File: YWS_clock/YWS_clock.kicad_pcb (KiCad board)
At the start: 2 copper layers, 140 x 90 mm, 60 parts, among them J1 Conn_01x06, J2 Power_inlet_vertical, J3 Conn_01x06, J4 Conn_01x06, SW1 Omron_B3F_SPST, SW2 Omron_B3F_SPST, SW3 Omron_B3F_SPST, SW4 Omron_B3F_SPST, U1 L7805, U2 ATmega328-PU, U3 DS1307_DIP-8, U4 MAX7219, U5 MAX7219, U6 MAX7219, U7 MAX7219, Y1 Crystal_16MHz, Y2 Crystal_16MHz

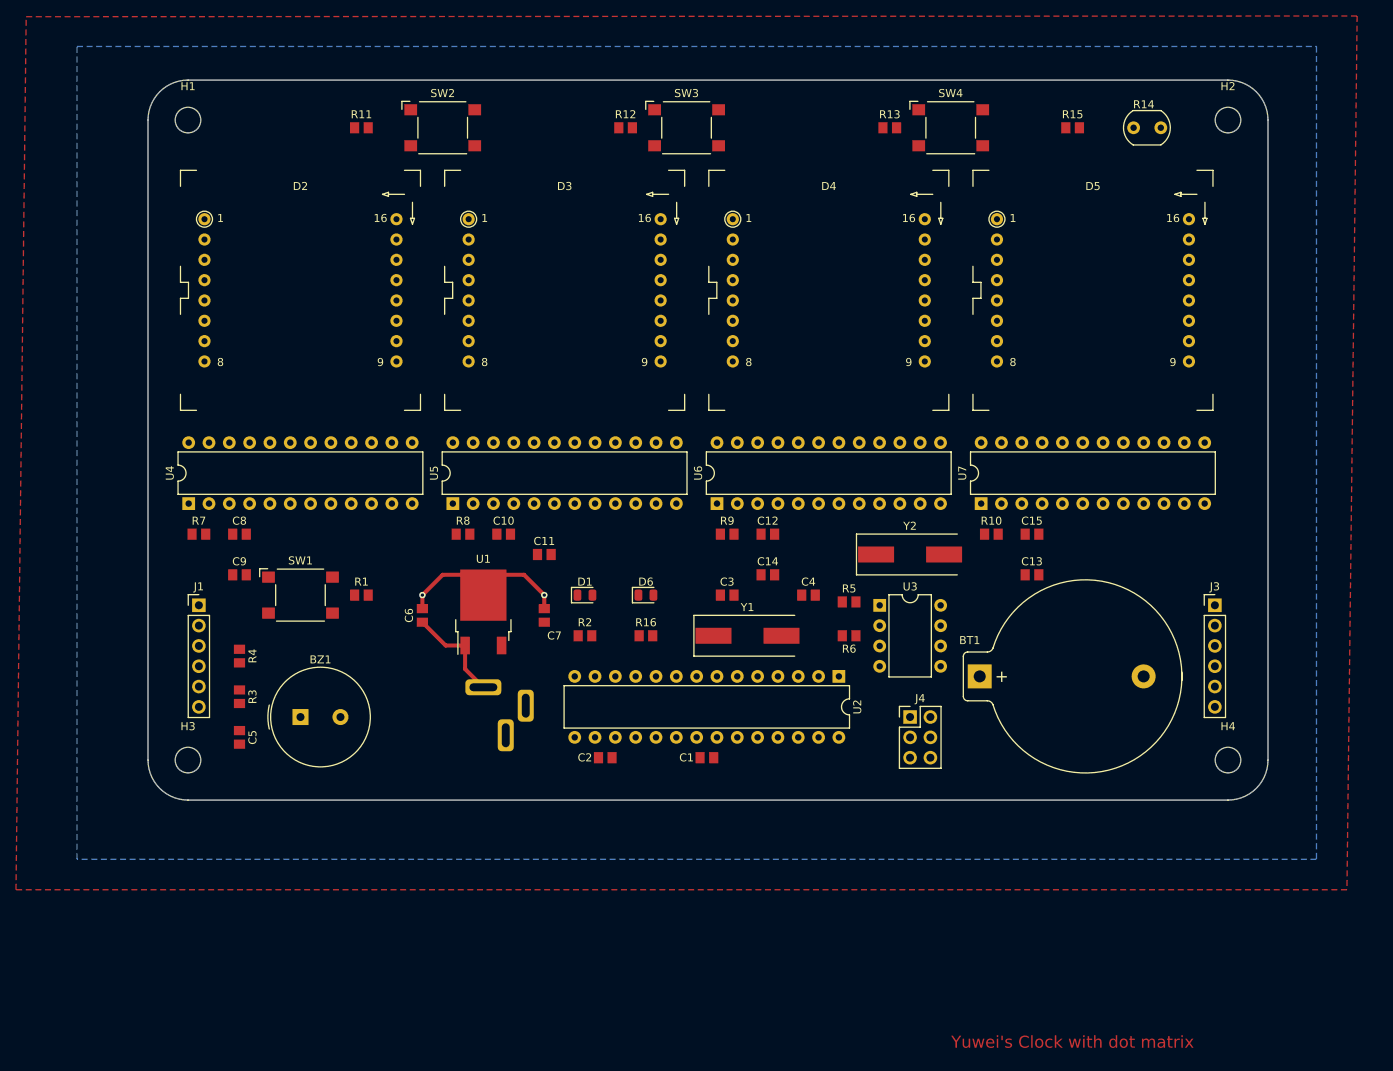
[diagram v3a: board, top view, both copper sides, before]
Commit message: Initial version with full routing and test point
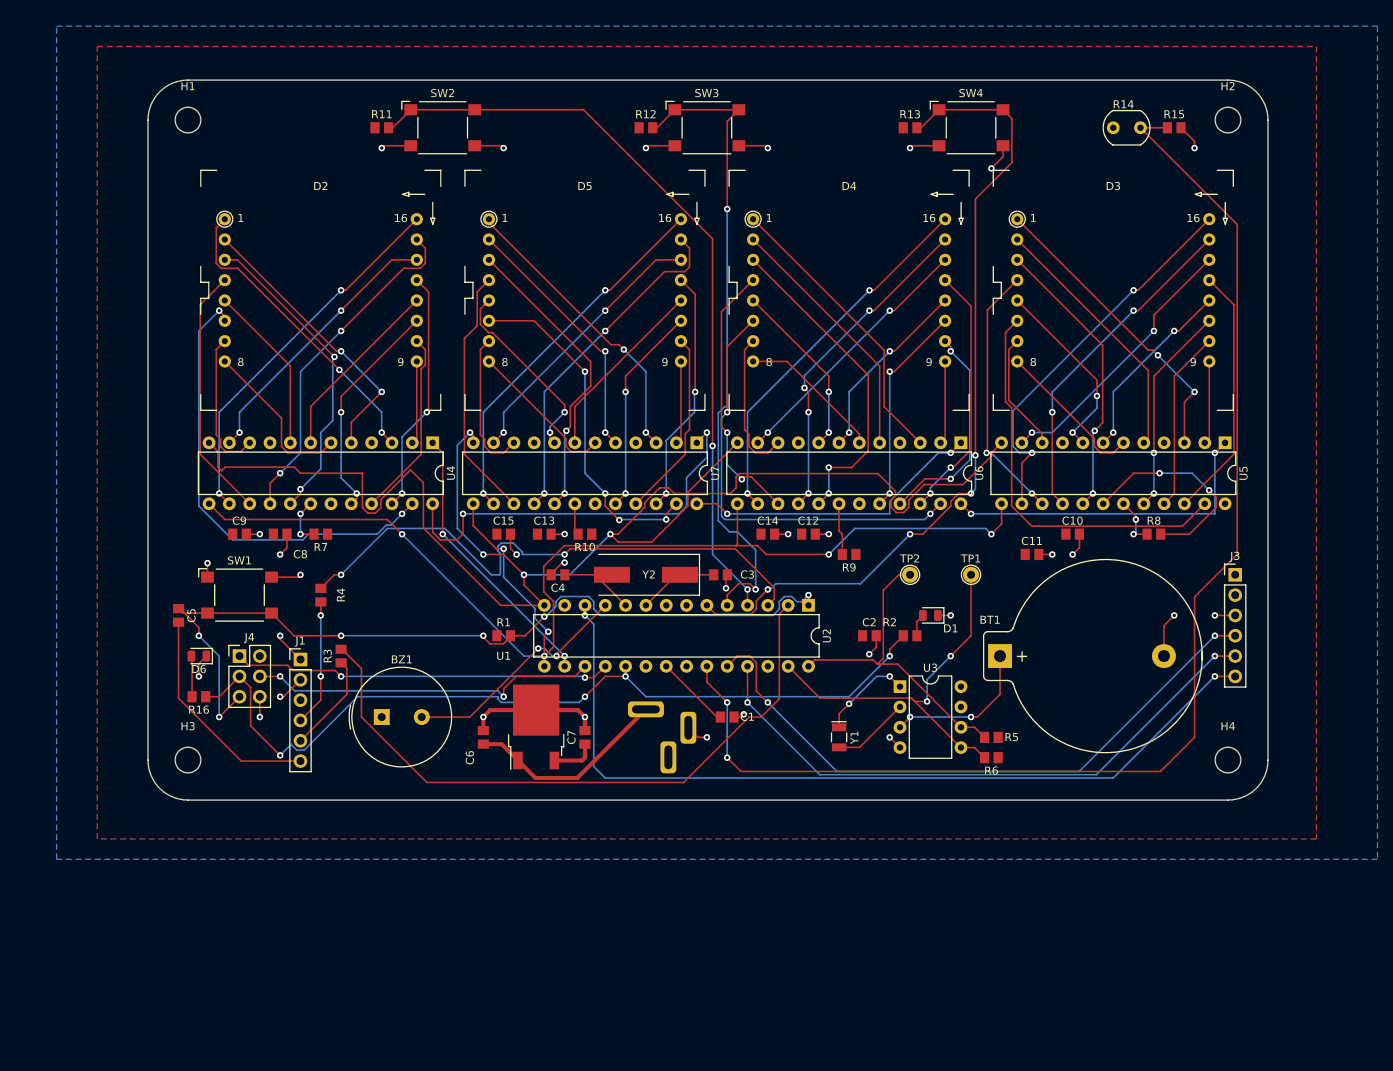
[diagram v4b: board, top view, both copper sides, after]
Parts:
- added TP1: TestPoint, footprints:TestPoint_THTPad_D2.0mm_Drill1.0mm, F.Cu at (182.9, 116.8)
- added TP2: TestPoint, footprints:TestPoint_THTPad_D2.0mm_Drill1.0mm, F.Cu at (175.3, 116.8)
- Y1: value Crystal_16MHz -> Crystal_32768Hz; footprint footprints:Crystal_SMD_HC49-SD -> footprints:Crystal_SMD_2Pin_3.2x1.5mm
- moved U5 96.8 mm to (214.6, 100.3), turned to -90 degrees
- moved R8 86.4 mm to (205.7, 111.8)
- moved J4 84.2 mm to (91.4, 127.0)
- moved C10 71.1 mm to (195.6, 111.8)
- moved D3 68.6 mm to (200.7, 81.3)
- moved C15 66.0 mm to (124.5, 111.8)
- moved D5 63.5 mm to (134.6, 81.3)
- moved C13 61.2 mm to (129.5, 111.8)
- moved C11 61.0 mm to (190.5, 114.3)
- moved D6 56.4 mm to (86.4, 127.0), turned to 180 degrees
- moved R16 56.4 mm to (86.4, 132.1), turned to 180 degrees
- moved R10 50.8 mm to (134.6, 111.8), turned to 180 degrees
- moved D1 43.3 mm to (177.8, 121.9), turned to 180 degrees
- moved R2 40.6 mm to (175.3, 124.5)
- moved C2 36.4 mm to (170.2, 124.5)
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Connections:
- J3 pad 6: JOYST_Z -> JOYST_SW
- J4 pad 1: MISD -> MISO
- J4 pad 4: MDSI -> MOSI
- U2 pad 11: JOYST_X -> BUZZER
- U2 pad 12: JOYST_Y -> JOYST_SW
- U2 pad 13: JOYST_Z -> unconnected-(U2-Pad13)
- U2 pad 24: BUZZER -> JOYST_X
- U2 pad 25: unconnected-(U2-Pad25) -> JOYST_Y
- Y1 pad 1: Net-(C3-Pad1) -> Net-(U3-Pad1)
- Y1 pad 2: Net-(C4-Pad1) -> Net-(U3-Pad2)
- Y2 pad 1: Net-(U3-Pad1) -> Net-(C3-Pad1)
- Y2 pad 2: Net-(U3-Pad2) -> Net-(C4-Pad1)
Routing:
- net DISP_LOAD: track 0.00 -> 189.8 mm, vias 0 -> 4
- net LIGHT_SENSOR: track 0.00 -> 160.2 mm, vias 0 -> 2
- net DISP_CLK: track 0.00 -> 157.0 mm, vias 0 -> 6
- net RESET: track 0.00 -> 107.8 mm, vias 0 -> 6
- net JOYST_SW: track 0.00 -> 106.6 mm, vias 0 -> 2
- net LED_SCK: track 0.00 -> 106.6 mm, vias 0 -> 4
- net BTN_DOWN: track 0.00 -> 103.3 mm, vias 0 -> 4
- net BTN_SEL: track 0.00 -> 95.7 mm, vias 0 -> 2
- net RXD: track 0.00 -> 81.7 mm
- net BTN_UP: track 0.00 -> 81.1 mm, vias 0 -> 2
- net JOYST_X: track 0.00 -> 79.1 mm, vias 0 -> 2
- net GND: track 22.8 -> 100.2 mm, vias 2 -> 32
- net JOYST_Y: track 0.00 -> 75.4 mm, vias 0 -> 2
- net TXD: track 0.00 -> 71.9 mm, vias 0 -> 2
- net Net-(D2-Pad6): track 0.00 -> 57.3 mm, vias 0 -> 2
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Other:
- board text removed: "Yuwei's Clock with dot matrix"

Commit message: Update with gerbers and BOM
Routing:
- net LED_SCK: track 106.6 -> 105.6 mm
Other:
- board text added: "RedSun"
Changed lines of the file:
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@@
     )
     (pad_to_mask_clearance 0)
+    (aux_axis_origin 78.74 144.78)
     (pcbplotparams
       (layerselection 0x00010fc_ffffffff)
@@
       (viasonmask false)
       (mode 1)
-      (useauxorigin false)
+      (useauxorigin true)
       (hpglpennumber 1)
       (hpglpenspeed 20)
@@
       (psa4output false)
       (plotreference true)
-      (plotvalue true)
+      (plotvalue false)
       (plotinvisibletext false)
       (sketchpadsonfab false)
-      (subtractmaskfromsilk false)
+      (subtractmaskfromsilk true)
       (outputformat 1)
       (mirror false)
-      (drillshape 1)
+      (drillshape 0)
       (scaleselection 1)
       (outputdirectory "")
@@
   (gr_line locked (start 210.6 57) (end 150 57) (layer "User.4") (width 0.05))
   (gr_line locked (start 82 64.4) (end 85 64.4) (layer "User.4") (width 0.05))
+  (gr_text "RedSun" (at 111.76 119.38) (layer "F.Cu")
+    (effects (font (size 2.286 2.286) (thickness 0.3) italic))
+  )
   (segment (start 95.44 117.13) (end 98.77 117.13) (width 0.2032) (layer "F.Cu") (net 1))
   (segment (start 152.252809 117.007191) (end 152.42 116.84) (width 0.2032) (layer "F.Cu") (net 1))
@@
   (segment (start 132.1 116.84) (end 135.88 116.84) (width 0.2032) (layer "F.Cu") (net 7))
   (segment (start 122.730689 125.464311) (end 124.430689 125.464311) (width 0.2032) (layer "F.Cu") (net 8))
-  (segment (start 91.44 132.08) (end 88.9 134.62) (width 0.2032) (layer "F.Cu") (net 8))
   (segment (start 125.31 124.585) (end 125.31 124.46) (width 0.2032) (layer "F.Cu") (net 8))
   (segment (start 84.003622 121.07) (end 83.82 121.07) (width 0.2032) (layer "F.Cu") (net 8))
@@
   (segment (start 127.149103 124.46) (end 129.54 122.069103) (width 0.2032) (layer "F.Cu") (net 8))
   (segment (start 124.430689 125.464311) (end 125.31 124.585) (width 0.2032) (layer "F.Cu") (net 8))
+  (segment (start 91.44 132.08) (end 88.9 134.62) (width 0.2032) (layer "F.Cu") (net 8))
   (segment (start 121.92 124.46) (end 121.92 124.653622) (width 0.2032) (layer "F.Cu") (net 8))
   (segment (start 87.44 121.63) (end 84.38 121.63) (width 0.2032) (layer "F.Cu") (net 8))
@@
   (segment (start 158.113111 121.92) (end 158.915689 121.117422) (width 0.2032) (layer "B.Cu") (net 8))
   (segment (start 129.54 122.069103) (end 129.69263 122.069103) (width 0.2032) (layer "B.Cu") (net 8))
+  (segment (start 88.9 127) (end 86.36 124.46) (width 0.2032) (layer "B.Cu") (net 8))
+  (segment (start 88.9 134.62) (end 88.9 127) (width 0.2032) (layer "B.Cu") (net 8))
   (segment (start 160.477422 119.555689) (end 161.124311 120.202578) (width 0.2032) (layer "B.Cu") (net 8))
   (segment (start 135.077422 119.555689) (end 135.724311 120.202578) (width 0.2032) (layer "B.Cu") (net 8))
@@
   (segment (start 131.622578 119.555689) (end 135.077422 119.555689) (width 0.2032) (layer "B.Cu") (net 8))
   (segment (start 104.14 124.46) (end 121.92 124.46) (width 0.2032) (layer "B.Cu") (net 8))
-  (segment (start 88.9 134.62) (end 88.9 127) (width 0.2032) (layer "B.Cu") (net 8))
-  (segment (start 88.9 127) (end 86.36 124.46) (width 0.2032) (layer "B.Cu") (net 8))
   (segment (start 158.915689 121.117422) (end 158.915689 120.202578) (width 0.2032) (layer "B.Cu") (net 8))
   (segment (start 161.124311 120.202578) (end 161.737422 120.202578) (width 0.2032) (layer "B.Cu") (net 8))
@@
   (segment (start 88.9 132.08) (end 91.44 129.54) (width 0.2032) (layer "F.Cu") (net 82))
   (segment (start 92.825689 130.925689) (end 92.825689 135.719989) (width 0.2032) (layer "F.Cu") (net 82))
+  (segment (start 92.825689 135.719989) (end 93.98 136.8743) (width 0.2032) (layer "F.Cu") (net 82))
   (segment (start 137.16 129.54) (end 139.7 129.54) (width 0.2032) (layer "F.Cu") (net 82))
   (segment (start 87.21 132.08) (end 88.9 132.08) (width 0.2032) (layer "F.Cu") (net 82))
   (segment (start 134.62 132.08) (end 137.16 129.54) (width 0.2032) (layer "F.Cu") (net 82))
-  (segment (start 92.825689 135.719989) (end 96.52 139.4143) (width 0.2032) (layer "F.Cu") (net 82))
+  (segment (start 93.98 136.8743) (end 93.98 137.16) (width 0.2032) (layer "F.Cu") (net 82))
   (segment (start 172.72 126.15) (end 172.72 127) (width 0.2032) (layer "F.Cu") (net 82))
   (segment (start 139.7 129.54) (end 139.7 128.28) (width 0.2032) (layer "F.Cu") (net 82))
@@
   (via (at 139.7 129.54) (size 0.8128) (drill 0.4064) (layers "F.Cu" "B.Cu") (net 82))
   (via (at 134.62 132.08) (size 0.8128) (drill 0.4064) (layers "F.Cu" "B.Cu") (net 82))
-  (via (at 96.52 139.4143) (size 0.8128) (drill 0.4064) (layers "F.Cu" "B.Cu") (net 82))
+  (via (at 93.98 137.16) (size 0.8128) (drill 0.4064) (layers "F.Cu" "B.Cu") (net 82))
   (via (at 172.72 127) (size 0.8128) (drill 0.4064) (layers "F.Cu" "B.Cu") (net 82))
   (segment (start 172.72 127) (end 167.64 132.08) (width 0.2032) (layer "B.Cu") (net 82))
   (segment (start 142.24 132.08) (end 139.7 129.54) (width 0.2032) (layer "B.Cu") (net 82))
+  (segment (start 99.538132 138.739311) (end 106.197443 132.08) (width 0.2032) (layer "B.Cu") (net 82))
+  (segment (start 95.559311 138.739311) (end 99.538132 138.739311) (width 0.2032) (layer "B.Cu") (net 82))
+  (segment (start 124.165613 132.790711) (end 133.909289 132.790711) (width 0.2032) (layer "B.Cu") (net 82))
+  (segment (start 123.749289 132.08) (end 123.749289 132.374387) (width 0.2032) (layer "B.Cu") (net 82))
+  (segment (start 167.64 132.08) (end 142.24 132.08) (width 0.2032) (layer "B.Cu") (net 82))
   (segment (start 106.197443 132.08) (end 123.749289 132.08) (width 0.2032) (layer "B.Cu") (net 82))
+  (segment (start 93.98 137.16) (end 95.559311 138.739311) (width 0.2032) (layer "B.Cu") (net 82))
   (segment (start 133.909289 132.790711) (end 134.62 132.08) (width 0.2032) (layer "B.Cu") (net 82))
-  (segment (start 97.905689 138.063132) (end 98.581868 138.739311) (width 0.2032) (layer "B.Cu") (net 82))
-  (segment (start 167.64 132.08) (end 142.24 132.08) (width 0.2032) (layer "B.Cu") (net 82))
-  (segment (start 98.581868 138.739311) (end 99.538132 138.739311) (width 0.2032) (layer "B.Cu") (net 82))
-  (segment (start 99.538132 138.739311) (end 106.197443 132.08) (width 0.2032) (layer "B.Cu") (net 82))
   (segment (start 123.749289 132.374387) (end 124.165613 132.790711) (width 0.2032) (layer "B.Cu") (net 82))
-  (segment (start 123.749289 132.08) (end 123.749289 132.374387) (width 0.2032) (layer "B.Cu") (net 82))
-  (segment (start 96.52 139.4143) (end 97.905689 138.028611) (width 0.2032) (layer "B.Cu") (net 82))
-  (segment (start 124.165613 132.790711) (end 133.909289 132.790711) (width 0.2032) (layer "B.Cu") (net 82))
-  (segment (start 97.905689 138.028611) (end 97.905689 138.063132) (width 0.2032) (layer "B.Cu") (net 82))
   (segment (start 155.133622 134.62) (end 146.955302 142.79832) (width 0.2032) (layer "F.Cu") (net 83))
   (segment (start 104.265 126.15) (end 104.14 126.15) (width 0.2032) (layer "F.Cu") (net 83))

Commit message: live review update
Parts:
- added R17: R_0805_47, footprints:R_0805_2012Metric, F.Cu at (118.0, 128.0)
- C7: value C_0805_1uf -> C_0805_0.1uf
- J4: value Conn_01x06 -> Conn_02x03_Odd_Even
- moved R7 2.07 mm to (103.7, 111.8), turned to 0 degrees
- moved R4 2.02 mm to (103.5, 120.0)
- moved C8 0.24 mm to (96.5, 112.0), turned to -90 degrees
- moved C9 0.07 mm to (91.4, 111.8), turned to -90 degrees
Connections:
- BZ1 pad 2: BUZZER -> Net-(BZ1-Pad2)
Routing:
- net DISP_LOAD: track 189.8 -> 220.9 mm, vias 4 -> 6
- net Net-(D3-Pad1): track 38.0 -> 52.0 mm, vias 2 -> 1
- net TXD: track 71.9 -> 62.3 mm, vias 2 -> 4
- net Net-(BZ1-Pad2): track 0.00 -> 7.83 mm
- net BUZZER: track 29.7 -> 22.3 mm
- net Net-(U4-Pad24): track 51.0 -> 44.7 mm
- net Net-(D2-Pad8): track 20.6 -> 25.5 mm, vias 0 -> 3
- net Net-(D2-Pad4): track 31.8 -> 36.7 mm
- net LED_SCK: track 105.6 -> 109.6 mm
- net Net-(D3-Pad11): track 26.3 -> 30.3 mm, vias 2 -> 1
- net Net-(D2-Pad7): track 18.2 -> 14.9 mm
- net DISP_CLK: track 157.0 -> 160.1 mm, vias 6 -> 5
- net Net-(R7-Pad2): track 6.03 -> 9.06 mm, vias 2 -> 1
- net Net-(D2-Pad16): track 46.7 -> 49.6 mm, vias 2 -> 1
- net Net-(D5-Pad6): track 43.4 -> 45.9 mm
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
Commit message: Final version for final review
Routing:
- net RESET: track 107.8 -> 110.1 mm, vias 6 -> 8
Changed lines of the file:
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@@
   (segment (start 125.31 124.585) (end 125.31 124.46) (width 0.2032) (layer "F.Cu") (net 8))
   (segment (start 84.003622 121.07) (end 83.82 121.07) (width 0.2032) (layer "F.Cu") (net 8))
-  (segment (start 98.27 124.46) (end 104.14 124.46) (width 0.2032) (layer "F.Cu") (net 8))
+  (segment (start 89 122) (end 87.81 122) (width 0.2032) (layer "F.Cu") (net 8))
   (segment (start 86.36 123.426378) (end 84.003622 121.07) (width 0.2032) (layer "F.Cu") (net 8))
   (segment (start 121.92 124.653622) (end 122.730689 125.464311) (width 0.2032) (layer "F.Cu") (net 8))
   (segment (start 84.38 121.63) (end 83.82 121.07) (width 0.2032) (layer "F.Cu") (net 8))
-  (segment (start 95.44 121.63) (end 98.27 124.46) (width 0.2032) (layer "F.Cu") (net 8))
-  (segment (start 95.44 121.63) (end 87.44 121.63) (width 0.2032) (layer "F.Cu") (net 8))
+  (segment (start 97 120.07) (end 97 120) (width 0.2032) (layer "F.Cu") (net 8))
   (segment (start 162.56 119.38) (end 162.56 120.66) (width 0.2032) (layer "F.Cu") (net 8))
   (segment (start 127.149103 124.46) (end 129.54 122.069103) (width 0.2032) (layer "F.Cu") (net 8))
@@
   (segment (start 91.44 132.08) (end 88.9 134.62) (width 0.2032) (layer "F.Cu") (net 8))
   (segment (start 121.92 124.46) (end 121.92 124.653622) (width 0.2032) (layer "F.Cu") (net 8))
+  (segment (start 95.44 121.63) (end 94.37 121.63) (width 0.2032) (layer "F.Cu") (net 8))
+  (segment (start 87.81 122) (end 87.44 121.63) (width 0.2032) (layer "F.Cu") (net 8))
   (segment (start 87.44 121.63) (end 84.38 121.63) (width 0.2032) (layer "F.Cu") (net 8))
+  (segment (start 95.44 121.63) (end 97 120.07) (width 0.2032) (layer "F.Cu") (net 8))
+  (segment (start 94.37 121.63) (end 94 122) (width 0.2032) (layer "F.Cu") (net 8))
   (segment (start 125.31 124.46) (end 127.149103 124.46) (width 0.2032) (layer "F.Cu") (net 8))
   (segment (start 86.36 124.46) (end 86.36 123.426378) (width 0.2032) (layer "F.Cu") (net 8))
@@
   (via (at 129.54 122.069103) (size 0.8128) (drill 0.4064) (layers "F.Cu" "B.Cu") (net 8))
   (via (at 88.9 134.62) (size 0.8128) (drill 0.4064) (layers "F.Cu" "B.Cu") (net 8))
-  (via (at 104.14 124.46) (size 0.8128) (drill 0.4064) (layers "F.Cu" "B.Cu") (net 8))
   (via (at 86.36 124.46) (size 0.8128) (drill 0.4064) (layers "F.Cu" "B.Cu") (net 8))
+  (via (at 94 122) (size 0.8128) (drill 0.4064) (layers "F.Cu" "B.Cu") (net 8))
   (via (at 121.92 124.46) (size 0.8128) (drill 0.4064) (layers "F.Cu" "B.Cu") (net 8))
+  (via (at 97 120) (size 0.8128) (drill 0.4064) (layers "F.Cu" "B.Cu") (net 8))
+  (via (at 89 122) (size 0.8128) (drill 0.4064) (layers "F.Cu" "B.Cu") (net 8))
   (segment (start 158.915689 120.202578) (end 159.562578 119.555689) (width 0.2032) (layer "B.Cu") (net 8))
   (segment (start 135.724311 120.202578) (end 135.724311 121.117422) (width 0.2032) (layer "B.Cu") (net 8))
@@
   (segment (start 160.477422 119.555689) (end 161.124311 120.202578) (width 0.2032) (layer "B.Cu") (net 8))
   (segment (start 135.077422 119.555689) (end 135.724311 120.202578) (width 0.2032) (layer "B.Cu") (net 8))
+  (segment (start 100.685098 120) (end 104.14 123.454902) (width 0.2032) (layer "B.Cu") (net 8))
   (segment (start 130.975689 120.202578) (end 131.622578 119.555689) (width 0.2032) (layer "B.Cu") (net 8))
   (segment (start 161.737422 120.202578) (end 162.56 119.38) (width 0.2032) (layer "B.Cu") (net 8))
@@
   (segment (start 131.622578 119.555689) (end 135.077422 119.555689) (width 0.2032) (layer "B.Cu") (net 8))
   (segment (start 104.14 124.46) (end 121.92 124.46) (width 0.2032) (layer "B.Cu") (net 8))
+  (segment (start 97 120) (end 100.685098 120) (width 0.2032) (layer "B.Cu") (net 8))
+  (segment (start 94 122) (end 89 122) (width 0.2032) (layer "B.Cu") (net 8))
   (segment (start 158.915689 121.117422) (end 158.915689 120.202578) (width 0.2032) (layer "B.Cu") (net 8))
+  (segment (start 104.14 123.454902) (end 104.14 124.46) (width 0.2032) (layer "B.Cu") (net 8))
   (segment (start 161.124311 120.202578) (end 161.737422 120.202578) (width 0.2032) (layer "B.Cu") (net 8))
   (segment (start 130.975689 120.786044) (end 130.975689 120.202578) (width 0.2032) (layer "B.Cu") (net 8))
@@
   (segment (start 99.06 137.585) (end 104.850711 131.794289) (width 0.2032) (layer "F.Cu") (net 75))
   (segment (start 99.06 135.045) (end 101.6 132.505) (width 0.2032) (layer "F.Cu") (net 76))
-  (segment (start 103.52 120.85) (end 102.45 121.92) (width 0.2032) (layer "F.Cu") (net 76))
+  (segment (start 101.6 125) (end 101.6 122.77) (width 0.2032) (layer "F.Cu") (net 76))
   (segment (start 101.6 132.505) (end 101.6 129.54) (width 0.2032) (layer "F.Cu") (net 76))
-  (segment (start 102.45 121.92) (end 101.6 121.92) (width 0.2032) (layer "F.Cu") (net 76))
+  (segment (start 101.6 122.77) (end 103.52 120.85) (width 0.2032) (layer "F.Cu") (net 76))
   (via (at 101.6 129.54) (size 0.8128) (drill 0.4064) (layers "F.Cu" "B.Cu") (net 76))
-  (via (at 101.6 121.92) (size 0.8128) (drill 0.4064) (layers "F.Cu" "B.Cu") (net 76))
-  (segment (start 101.6 121.92) (end 101.6 129.54) (width 0.2032) (layer "B.Cu") (net 76))
+  (via (at 101.6 125) (size 0.8128) (drill 0.4064) (layers "F.Cu" "B.Cu") (net 76))
+  (segment (start 101.6 125) (end 101.6 129.54) (width 0.2032) (layer "B.Cu") (net 76))
   (segment (start 155.221733 127) (end 153.68 127) (width 0.2032) (layer "F.Cu") (net 78))
   (segment (start 156.044311 127.822578) (end 155.221733 127) (width 0.2032) (layer "F.Cu") (net 78))
